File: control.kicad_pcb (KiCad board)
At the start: 4 copper layers, 111.9 x 109.5 mm, 187 parts, among them J1 Wurth_THR_Terminal_M4, J10 Conn_02x20_Odd_Even, J11 Conn_ARM_JTAG_SWD_10, J12 TE_Faston_20-16AWG_Straight_T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, J13 TE_Faston_20-16AWG_Straight_T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, J14 TE_Faston_20-16AWG_Straight_T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, J15 TE_Faston_20-16AWG_Straight_T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, J16 TE_Faston_20-16AWG_Straight_T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, J17 TE_Faston_20-16AWG_Straight_T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, J18 TE_Faston_20-16AWG_Straight_T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, J19 TE_Faston_20-16AWG_Straight_T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, J2 Wurth_THR_Terminal_M4, J20 TE_Faston_20-16AWG_Straight_T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, J21 TE_Faston_20-16AWG_Straight_T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, J22 TE_Faston_20-16AWG_Straight_T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, J23 TE_Faston_20-16AWG_Straight_T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, J24 TE_Faston_20-16AWG_Straight_T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, J25 TE_Faston_20-16AWG_Straight_T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, J26 TE_Faston_20-16AWG_Straight_T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, J27 TE_Faston_20-16AWG_Straight_T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, J28 Conn_01x02, J3 Conn_02x08_Odd_Even, J4 Conn_02x08_Odd_Even, J5 Conn_02x08_Odd_Even, J6 Conn_02x08_Odd_Even, J7 Conn_02x08_Odd_Even, SW1 SW_Push, U1 TPS7B8733, U10 PCA9358, U2 MAX33071, U3 ATSAMD21J18A-A, U4 TCMT4600, U5 TCMT4600, U6 TCMT4600, U7 TCMT4600, U8 TCMT4600, U9 TCMT4600, Y1 32.768kHz

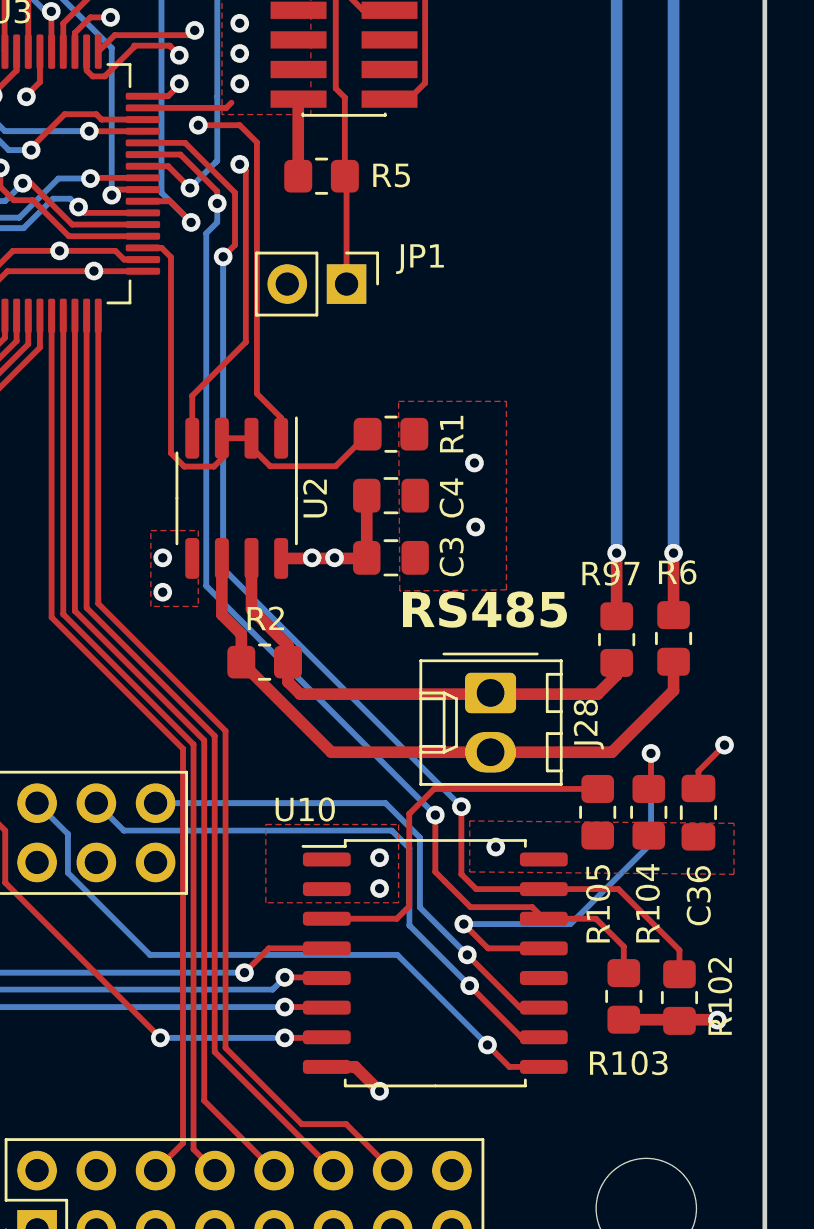
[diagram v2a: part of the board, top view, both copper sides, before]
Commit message: generate pedigree B
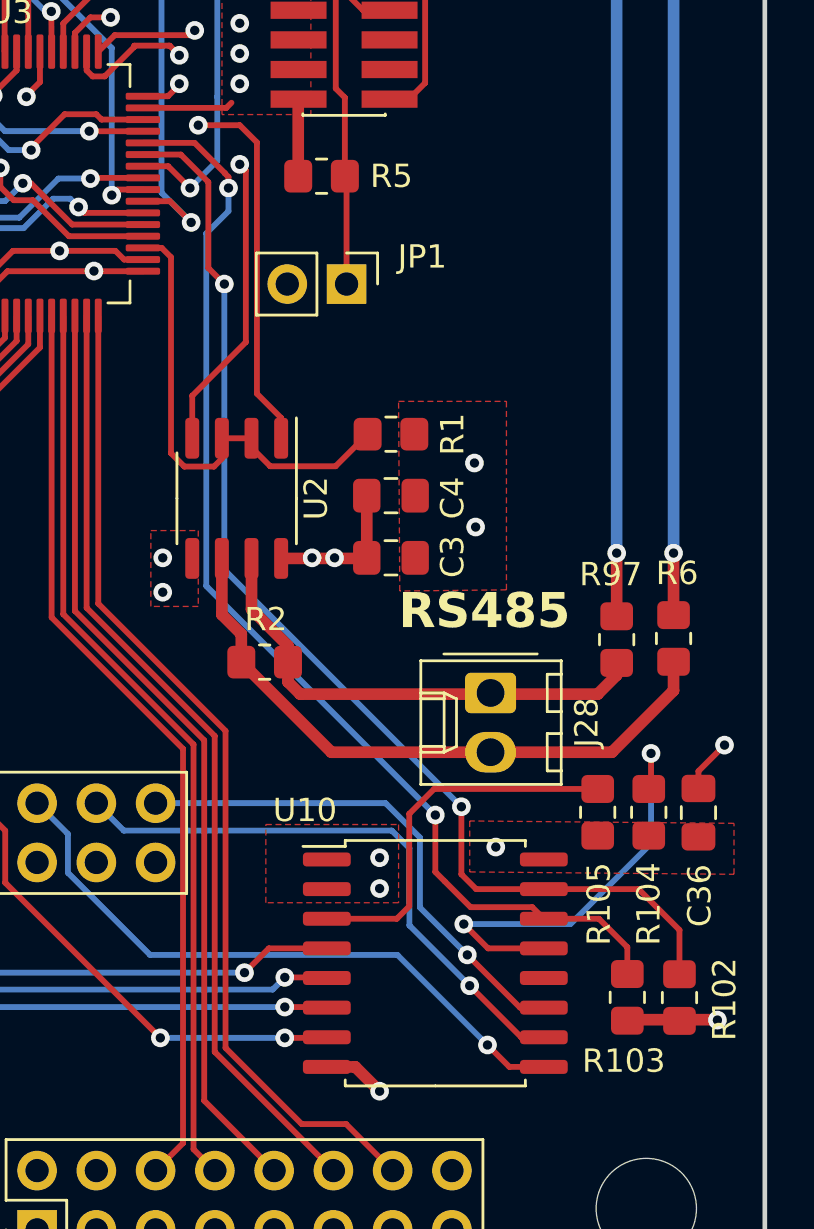
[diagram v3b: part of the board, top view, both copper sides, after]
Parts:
- R102: renamed from R103; value 39 -> 4.7k
- R103: renamed from R102; value 39 -> 4.7k
- moved R102 2.39 mm to (179.2, 137.9)
- moved R103 2.24 mm to (176.9, 137.9)
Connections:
- R102 pad 1: I2C3_SCL -> I2C3_SDA
- R103 pad 1: I2C3_SDA -> I2C3_SCL
- U3 pad 43: I2C3_SCL -> I2C3_SDA
- U3 pad 44: I2C3_SDA -> I2C3_SCL
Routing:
- net I2C3_SCL: track 48.1 -> 49.5 mm
- net I2C3_SDA: track 50.2 -> 49.7 mm
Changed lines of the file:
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@@
       (sketchpadsonfab false)
       (subtractmaskfromsilk false)
-      (outputformat 1)
+      (outputformat 4)
       (mirror false)
       (drillshape 0)
       (scaleselection 1)
-      (outputdirectory "out/ped_a/")
+      (outputdirectory "out/ped_b")
     )
   )
@@
   )
   (footprint "Resistor_SMD:R_0805_2012Metric_Pad1.20x1.40mm_HandSolder" (layer "F.Cu")
-    (at 176.784 137.8204 -90)
+    (at 179.1716 137.8712 -90)
     (descr "Resistor SMD 0805 (2012 Metric), square (rectangular) end terminal, IPC_7351 nominal with elongated pad for handsoldering. (Body size source: IPC-SM-782 page 72, https://www.pcb-3d.com/wordpress/wp-content/uploads/ipc-sm-782a_amendment_1_and_2.pdf), generated with kicad-footprint-generator")
     (tags "resistor handsolder")
@@
     (property "ki_keywords" "R res resistor")
     (attr smd)
-    (fp_text reference "R103" (at 2.8956 -0.2032 -180) (layer "F.SilkS")
+    (fp_text reference "R102" (at 0.0762 -1.9304 -90) (layer "F.SilkS")
         (effects (font (size 1 1) (thickness 0.15)))
     )
-    (fp_text value "39" (at 0 1.65 90) (layer "F.Fab")
+    (fp_text value "4.7k" (at 0 1.65 90) (layer "F.Fab")
         (effects (font (size 1 1) (thickness 0.15)))
     )
@@
       (stroke (width 0.1) (type solid)) (layer "F.Fab"))
     (pad "1" smd roundrect (at -1 0 270) (size 1.2 1.4) (layers "F.Cu" "F.Paste" "F.Mask") (roundrect_rratio 0.2083333333)
-      (net 135 "I2C3_SCL") (pintype "passive"))
+      (net 131 "I2C3_SDA") (pintype "passive"))
     (pad "2" smd roundrect (at 1 0 270) (size 1.2 1.4) (layers "F.Cu" "F.Paste" "F.Mask") (roundrect_rratio 0.2083333333)
       (net 4 "+3.3V") (pintype "passive"))
@@
       (net 29 "SIDE_DOOR_SENSE") (pinfunction "PA21") (pintype "bidirectional"))
     (pad "43" smd roundrect (at 5.6625 -1.25) (size 1.475 0.3) (layers "F.Cu" "F.Paste" "F.Mask") (roundrect_rratio 0.25)
-      (net 135 "I2C3_SCL") (pinfunction "PA22") (pintype "bidirectional"))
+      (net 131 "I2C3_SDA") (pinfunction "PA22") (pintype "bidirectional"))
     (pad "44" smd roundrect (at 5.6625 -1.75) (size 1.475 0.3) (layers "F.Cu" "F.Paste" "F.Mask") (roundrect_rratio 0.25)
-      (net 131 "I2C3_SDA") (pinfunction "PA23") (pintype "bidirectional"))
+      (net 135 "I2C3_SCL") (pinfunction "PA23") (pintype "bidirectional"))
     (pad "45" smd roundrect (at 5.6625 -2.25) (size 1.475 0.3) (layers "F.Cu" "F.Paste" "F.Mask") (roundrect_rratio 0.25)
       (net 15 "CAB_7_SENSE") (pinfunction "PA24") (pintype "bidirectional"))
@@
       (stroke (width 0.1) (type solid)) (layer "F.Fab"))
     (pad "1" smd roundrect (at -2.5 0) (size 3.5 1.8) (layers "F.Cu" "F.Paste" "F.Mask") (roundrect_rratio 0.1388888889)
-      (net 5 "+12V") (pinfunction "K") (pintype "passive"))
+      (net 5 "+12V") (pinfunction "K") (pintype "passive") (zone_connect 2))
     (pad "2" smd roundrect (at 2.5 0) (size 3.5 1.8) (layers "F.Cu" "F.Paste" "F.Mask") (roundrect_rratio 0.1388888889)
       (net 181 "Net-(D2-A)") (pinfunction "A") (pintype "passive"))
@@
   )
   (footprint "Resistor_SMD:R_0805_2012Metric_Pad1.20x1.40mm_HandSolder" (layer "F.Cu")
-    (at 179.1716 137.8712 -90)
+    (at 176.9364 137.8618 -90)
     (descr "Resistor SMD 0805 (2012 Metric), square (rectangular) end terminal, IPC_7351 nominal with elongated pad for handsoldering. (Body size source: IPC-SM-782 page 72, https://www.pcb-3d.com/wordpress/wp-content/uploads/ipc-sm-782a_amendment_1_and_2.pdf), generated with kicad-footprint-generator")
     (tags "resistor handsolder")
@@
     (property "ki_keywords" "R res resistor")
     (attr smd)
-    (fp_text reference "R102" (at -0.0508 -1.778 90) (layer "F.SilkS")
+    (fp_text reference "R103" (at 2.7272 0.1524 -180) (layer "F.SilkS")
         (effects (font (size 1 1) (thickness 0.15)))
     )
-    (fp_text value "39" (at 0 1.65 90) (layer "F.Fab")
+    (fp_text value "4.7k" (at 0 1.65 90) (layer "F.Fab")
         (effects (font (size 1 1) (thickness 0.15)))
     )
@@
       (stroke (width 0.1) (type solid)) (layer "F.Fab"))
     (pad "1" smd roundrect (at -1 0 270) (size 1.2 1.4) (layers "F.Cu" "F.Paste" "F.Mask") (roundrect_rratio 0.2083333333)
-      (net 131 "I2C3_SDA") (pintype "passive"))
+      (net 135 "I2C3_SCL") (pintype "passive"))
     (pad "2" smd roundrect (at 1 0 270) (size 1.2 1.4) (layers "F.Cu" "F.Paste" "F.Mask") (roundrect_rratio 0.2083333333)
       (net 4 "+3.3V") (pintype "passive"))
@@
   (segment (start 166.5732 129.54) (end 156.718 129.54) (width 0.25) (layer "B.Cu") (net 129))
   (segment (start 173.3568 133.223) (end 170.4594 133.223) (width 0.25) (layer "F.Cu") (net 131))
-  (segment (start 179.1716 136.8712) (end 179.1716 135.8392) (width 0.25) (layer "F.Cu") (net 131))
-  (segment (start 156.1735 101.24) (end 157.9836 101.24) (width 0.25) (layer "F.Cu") (net 131))
+  (segment (start 177.419 133.223) (end 173.3568 133.223) (width 0.25) (layer "F.Cu") (net 131))
+  (segment (start 158.9786 106.6038) (end 159.6644 107.2896) (width 0.25) (layer "F.Cu") (net 131))
+  (segment (start 157.7978 101.74) (end 158.9786 102.9208) (width 0.25) (layer "F.Cu") (net 131))
   (segment (start 170.4594 133.223) (end 169.8244 132.588) (width 0.25) (layer "F.Cu") (net 131))
   (segment (start 169.8244 132.588) (end 169.8244 129.6924) (width 0.25) (layer "F.Cu") (net 131))
-  (segment (start 157.9836 101.24) (end 160.1216 103.378) (width 0.25) (layer "F.Cu") (net 131))
-  (segment (start 176.5554 133.223) (end 173.3568 133.223) (width 0.25) (layer "F.Cu") (net 131))
-  (segment (start 179.1716 135.8392) (end 176.5554 133.223) (width 0.25) (layer "F.Cu") (net 131))
-  (segment (start 160.1216 103.378) (end 160.1216 105.6132) (width 0.25) (layer "F.Cu") (net 131))
-  (segment (start 160.1216 105.6132) (end 159.6136 106.1212) (width 0.25) (layer "F.Cu") (net 131))
+  (segment (start 179.1716 134.9756) (end 177.419 133.223) (width 0.25) (layer "F.Cu") (net 131))
+  (segment (start 179.1716 136.8712) (end 179.1716 134.9756) (width 0.25) (layer "F.Cu") (net 131))
+  (segment (start 158.9786 102.9208) (end 158.9786 106.6038) (width 0.25) (layer "F.Cu") (net 131))
+  (segment (start 156.1735 101.74) (end 157.7978 101.74) (width 0.25) (layer "F.Cu") (net 131))
+  (via (at 159.6644 107.2896) (size 0.8) (drill 0.4) (layers "F.Cu" "B.Cu") (net 131))
   (via (at 169.8244 129.6924) (size 0.8) (drill 0.4) (layers "F.Cu" "B.Cu") (free) (net 131))
-  (via (at 159.6136 106.1212) (size 0.8) (drill 0.4) (layers "F.Cu" "B.Cu") (net 131))
-  (segment (start 169.8244 129.6924) (end 159.6136 119.4816) (width 0.25) (layer "B.Cu") (net 131))
-  (segment (start 159.6136 119.4816) (end 159.6136 106.1212) (width 0.25) (layer "B.Cu") (net 131))
+  (segment (start 169.8244 129.6924) (end 159.7533 119.6213) (width 0.25) (layer "B.Cu") (net 131))
+  (segment (start 159.6644 119.5324) (end 159.7533 119.6213) (width 0.25) (layer "B.Cu") (net 131))
+  (segment (start 159.6644 107.2896) (end 159.6644 119.5324) (width 0.25) (layer "B.Cu") (net 131))
   (segment (start 168.7068 130.048) (end 168.7068 130.302) (width 0.25) (layer "F.Cu") (net 135))
-  (segment (start 159.3596 103.317895) (end 159.3596 103.8352) (width 0.25) (layer "F.Cu") (net 135))
-  (segment (start 157.781705 101.74) (end 159.3596 103.317895) (width 0.25) (layer "F.Cu") (net 135))
+  (segment (start 159.685147 102.535147) (end 159.685147 102.544452) (width 0.25) (layer "F.Cu") (net 135))
+  (segment (start 176.9364 135.7122) (end 175.7172 134.493) (width 0.25) (layer "F.Cu") (net 135))
+  (segment (start 159.685147 102.544452) (end 159.8422 102.701505) (width 0.25) (layer "F.Cu") (net 135))
   (segment (start 172.8604 133.9966) (end 170.217 133.9966) (width 0.25) (layer "F.Cu") (net 135))
-  (segment (start 176.784 135.6868) (end 176.784 136.8204) (width 0.25) (layer "F.Cu") (net 135))
+  (segment (start 156.1735 101.24) (end 158.39 101.24) (width 0.25) (layer "F.Cu") (net 135))
   (segment (start 169.1132 132.8928) (end 168.7068 132.4864) (width 0.25) (layer "F.Cu") (net 135))
-  (segment (start 156.1735 101.74) (end 157.781705 101.74) (width 0.25) (layer "F.Cu") (net 135))
   (segment (start 170.217 133.9966) (end 169.1132 132.8928) (width 0.25) (layer "F.Cu") (net 135))
-  (segment (start 175.5902 134.493) (end 176.784 135.6868) (width 0.25) (layer "F.Cu") (net 135))
+  (segment (start 176.9364 136.8618) (end 176.9364 135.7122) (width 0.25) (layer "F.Cu") (net 135))
   (segment (start 168.7068 132.4864) (end 168.7068 130.048) (width 0.25) (layer "F.Cu") (net 135))
-  (segment (start 173.3568 134.493) (end 175.5902 134.493) (width 0.25) (layer "F.Cu") (net 135))
+  (segment (start 159.8422 102.701505) (end 159.8422 103.1748) (width 0.25) (layer "F.Cu") (net 135))
   (segment (start 173.3568 134.493) (end 172.8604 133.9966) (width 0.25) (layer "F.Cu") (net 135))
+  (segment (start 175.7172 134.493) (end 173.3568 134.493) (width 0.25) (layer "F.Cu") (net 135))
+  (segment (start 158.39 101.24) (end 159.685147 102.535147) (width 0.25) (layer "F.Cu") (net 135))
   (via (at 168.7068 130.048) (size 0.8) (drill 0.4) (layers "F.Cu" "B.Cu") (net 135))
-  (via (at 159.3596 103.8352) (size 0.8) (drill 0.4) (layers "F.Cu" "B.Cu") (free) (net 135))
+  (via (at 159.8422 103.1748) (size 0.8) (drill 0.4) (layers "F.Cu" "B.Cu") (net 135))
+  (segment (start 159.8422 104.1654) (end 159.8422 103.1748) (width 0.25) (layer "B.Cu") (net 135))
   (segment (start 168.7068 130.048) (end 158.8886 120.2298) (width 0.25) (layer "B.Cu") (net 135))
-  (segment (start 159.3596 104.648) (end 159.3596 103.8352) (width 0.25) (layer "B.Cu") (net 135))
-  (segment (start 158.8886 105.119) (end 159.3596 104.648) (width 0.25) (layer "B.Cu") (net 135))
+  (segment (start 158.8886 105.119) (end 159.8422 104.1654) (width 0.25) (layer "B.Cu") (net 135))
   (segment (start 158.8886 120.2298) (end 158.8886 105.119) (width 0.25) (layer "B.Cu") (net 135))
   (segment (start 164.4396 98.9076) (end 164.83 99.298) (width 0.25) (layer "F.Cu") (net 142))
